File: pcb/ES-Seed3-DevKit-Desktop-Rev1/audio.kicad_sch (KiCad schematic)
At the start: 49 parts, among them J1 AudioJack3_Switch, J2 AudioJack3_Switch, J3 AudioJack3_Switch, J4 AudioJack3_Switch, J5 AudioJack3_Switch, U1 TPA6110A2DGN, U15 OPA1652, U3 OPA1652

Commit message: lsno ERC errors or warnings, the few leftover warnings are excluded with valid comments.
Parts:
- renumbered D1 to D21, D2 to D22, D3 to D23, D4 to D24
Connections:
- net GND: now also J1.S, J2.S, J3.S, J4.S
- net AUDIO_IN_RIGHT_DETECT: now reaches J2.SN
- net at J2.T: now also C9.2
- net at J2.TN: no longer C9.2
- net AUDIO_IN_LEFT_DETECT: now reaches J1.SN
- net at J1.T: now also C10.2
- net at J1.TN: no longer C10.2
- no-connect marks 3 -> 17
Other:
- moved on the sheet: J1, J2

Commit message: pre-routing checkpoint.
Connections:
- net CODEC_OUT_L: now also R61.2; no longer R96.2
- net CODEC_OUT_R: now also R96.2; no longer R61.2
- net at C12.2: now also J3.T; no longer J4.T
- net at C11.2: now also J4.T; no longer J3.T
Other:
- moved on the sheet: J3, J4
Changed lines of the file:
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@@
 	(global_label "CODEC_OUT_L"
 		(shape input)
-		(at 167.64 31.75 180)
+		(at 167.64 88.9 180)
 		(fields_autoplaced yes)
 		(effects
@@
 		)
 		(property "Intersheetrefs" "${INTERSHEET_REFS}"
-			(at 151.7734 31.75 0)
+			(at 151.5315 88.9 0)
 			(effects
 				(font
@@
 	(global_label "CODEC_OUT_R"
 		(shape input)
-		(at 167.64 88.9 180)
+		(at 167.64 31.75 180)
 		(fields_autoplaced yes)
 		(effects
@@
 		)
 		(property "Intersheetrefs" "${INTERSHEET_REFS}"
-			(at 151.5315 88.9 0)
+			(at 151.7734 31.75 0)
 			(effects
 				(font
@@
 	(symbol
 		(lib_id "Connector_Audio:AudioJack3_Switch")
-		(at 251.46 96.52 180)
+		(at 251.46 39.37 180)
 		(unit 1)
 		(exclude_from_sim no)
@@
 		(dnp no)
 		(property "Reference" "J4"
-			(at 253.365 107.95 0)
+			(at 253.365 50.8 0)
 			(effects
 				(font
@@
 		)
 		(property "Value" "AudioJack3_Switch"
-			(at 253.365 105.41 0)
+			(at 253.365 48.26 0)
 			(effects
 				(font
@@
 		)
 		(property "Footprint" "Connector_Audio:Jack_6.35mm_Neutrik_NMJ6HCD2_Horizontal"
-			(at 251.46 96.52 0)
+			(at 251.46 39.37 0)
 			(effects
 				(font
@@
 		)
 		(property "Datasheet" "~"
-			(at 251.46 96.52 0)
+			(at 251.46 39.37 0)
 			(effects
 				(font
@@
 		)
 		(property "Description" "Audio Jack, 3 Poles (Stereo / TRS), Switched Poles (Normalling)"
-			(at 251.46 96.52 0)
+			(at 251.46 39.37 0)
 			(effects
 				(font
@@
 	(symbol
 		(lib_id "Connector_Audio:AudioJack3_Switch")
-		(at 251.46 39.37 180)
+		(at 251.46 96.52 180)
 		(unit 1)
 		(exclude_from_sim no)
@@
 		(dnp no)
 		(property "Reference" "J3"
-			(at 253.365 50.8 0)
+			(at 253.365 107.95 0)
 			(effects
 				(font
@@
 		)
 		(property "Value" "AudioJack3_Switch"
-			(at 253.365 48.26 0)
+			(at 253.365 105.41 0)
 			(effects
 				(font
@@
 		)
 		(property "Footprint" "Connector_Audio:Jack_6.35mm_Neutrik_NMJ6HCD2_Horizontal"
-			(at 251.46 39.37 0)
+			(at 251.46 96.52 0)
 			(effects
 				(font
@@
 		)
 		(property "Datasheet" "~"
-			(at 251.46 39.37 0)
+			(at 251.46 96.52 0)
 			(effects
 				(font
@@
 		)
 		(property "Description" "Audio Jack, 3 Poles (Stereo / TRS), Switched Poles (Normalling)"
-			(at 251.46 39.37 0)
+			(at 251.46 96.52 0)
 			(effects
 				(font

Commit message: routed, productions mats, etc.
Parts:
- R63, R94: value 7K5 -> 20K
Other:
- note added: "I updated these to be gain of 2. However, I'm not really sure how the math works out for the other two values.. So, I may just need to kludge those a a bit IRL. (This can also be reworked to be our normal basic filter)"
- note removed: "TODO: Update values for gain of 2"
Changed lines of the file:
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@@
 	(text "Gain is set to target +4dBu (maximum)\nobviously this does not make it a pro-line-level device that way..\nwe'd need to probably have a certain amount of headroom.\nIf, instead we look at this as a -10dBV device, then we have\n~14dB of headroom with these values.\n\nGin=0.814 (Rin=10k, Rfb=16k)\nGout=1.228 (Rin=10k, Rfb=24k)\n\nAlternatively we can go closer to the PCM3060's \"2Vrms\" reference and just do:\nGin=0.5, Gout=2 :shrug:\n\nFor now, I've implemented the left channel of audio with less atten/gain."
 		(exclude_from_sim no)
-		(at 4.318 167.132 0)
+		(at 5.08 170.942 0)
 		(effects
 			(font
@@
 		)
 	)
-	(text "TODO: Update values for gain of 2"
+	(text "I updated these to be gain of 2.\nHowever, I'm not really sure how the math works out for the other two values..\nSo, I may just need to kludge those a a bit IRL.\n(This can also be reworked to be our normal basic filter)"
 		(exclude_from_sim no)
-		(at 162.814 22.098 0)
-		(effects
-			(font
-				(size 1.27 1.27)
-			)
-		)
-	)
-	(text "TODO: Update values for gain of 2"
-		(exclude_from_sim no)
-		(at 163.322 78.486 0)
+		(at 250.444 62.484 0)
 		(effects
 			(font
@@
 			)
 		)
-		(property "Value" "7K5"
+		(property "Value" "20K"
 			(at 196.85 66.04 90)
 			(effects
@@
 			)
 		)
-		(property "Value" "7K5"
+		(property "Value" "20K"
 			(at 196.85 8.89 90)
 			(effects

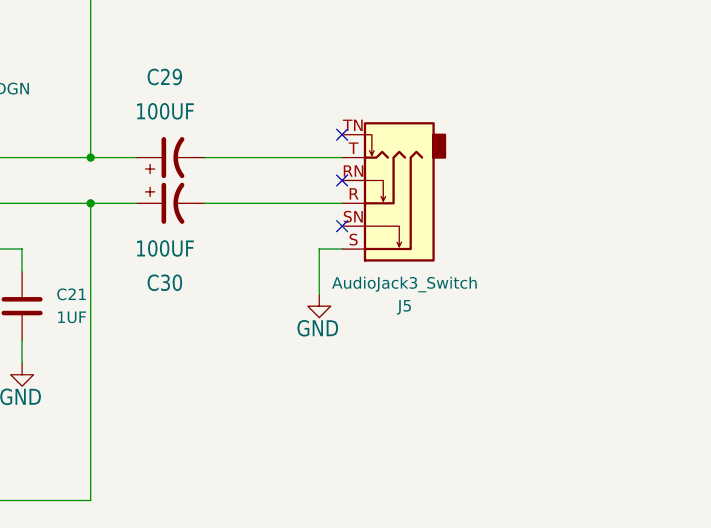
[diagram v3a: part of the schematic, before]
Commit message: slight sch tweaks for better bom parsing on jlcpcb.
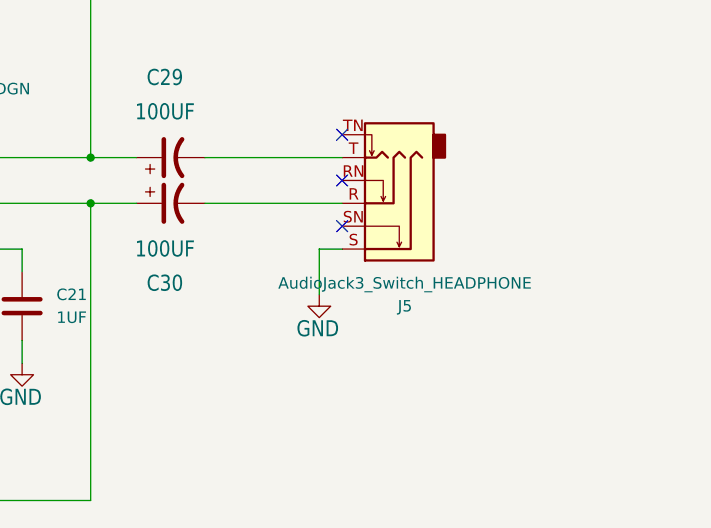
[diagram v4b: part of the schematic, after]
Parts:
- J5: value AudioJack3_Switch -> AudioJack3_Switch_HEADPHONE
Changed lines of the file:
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@@
 			)
 		)
-		(property "Value" "AudioJack3_Switch"
+		(property "Value" "AudioJack3_Switch_HEADPHONE"
 			(at 266.065 173.99 0)
 			(effects
